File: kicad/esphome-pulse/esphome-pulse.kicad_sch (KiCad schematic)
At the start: 3 parts, among them J2 AudioJack2_Ground

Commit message: Sent to production
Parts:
- removed D1: APA-106-F5, LED_THT:LED_D5.0mm-4_RGB_Staggered_Pins, symbol LED:APA-106-F5
- added D3: WS2812B_THT, LED_THT:LED_D5.0mm-4_RGB_Staggered_Pins, symbol LED:NeoPixel_THT
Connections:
- net +5V: now also D3.4 (VDD)
- net GND: now also D3.2 (GND)
- net at U1.9 (A1CH8/TCH9/GPIO9): now also D3.1 (DIN)
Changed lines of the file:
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@@
 	)
 	(junction
-		(at 193.04 114.3)
+		(at 193.04 123.19)
 		(diameter 0)
 		(color 0 0 0 0)
@@
 	)
 	(no_connect
-		(at 212.09 104.14)
-	)
-	(no_connect
 		(at 93.98 82.55)
 	)
@@
 	)
 	(no_connect
+		(at 212.09 109.22)
+	)
+	(no_connect
 		(at 160.02 93.98)
 	)
@@
 	(wire
 		(pts
-			(xy 179.07 43.18) (xy 179.07 104.14)
-		)
-		(stroke
-			(width 0)
-			(type default)
-		)
-	)
-	(wire
-		(pts
-			(xy 193.04 114.3) (xy 204.47 114.3)
+			(xy 193.04 123.19) (xy 204.47 123.19)
+		)
+		(stroke
+			(width 0)
+			(type default)
+		)
+	)
+	(wire
+		(pts
+			(xy 179.07 43.18) (xy 179.07 109.22)
 		)
 		(stroke
@@
 	(wire
 		(pts
-			(xy 179.07 104.14) (xy 196.85 104.14)
-		)
-		(stroke
-			(width 0)
-			(type default)
-		)
-	)
-	(wire
-		(pts
-			(xy 193.04 77.47) (xy 193.04 114.3)
+			(xy 193.04 123.19) (xy 193.04 143.51)
 		)
 		(stroke
@@
 	(wire
 		(pts
-			(xy 204.47 96.52) (xy 204.47 99.06)
+			(xy 204.47 116.84) (xy 204.47 123.19)
 		)
 		(stroke
@@
 	(wire
 		(pts
+			(xy 204.47 96.52) (xy 204.47 101.6)
+		)
+		(stroke
+			(width 0)
+			(type default)
+		)
+	)
+	(wire
+		(pts
 			(xy 129.54 143.51) (xy 193.04 143.51)
 		)
@@
 	(wire
 		(pts
+			(xy 179.07 109.22) (xy 196.85 109.22)
+		)
+		(stroke
+			(width 0)
+			(type default)
+		)
+	)
+	(wire
+		(pts
 			(xy 129.54 139.7) (xy 129.54 143.51)
 		)
@@
 	(wire
 		(pts
-			(xy 193.04 143.51) (xy 193.04 114.3)
+			(xy 193.04 77.47) (xy 193.04 123.19)
 		)
 		(stroke
@@
 	)
 	(symbol
-		(lib_id "LED:APA-106-F5")
-		(at 204.47 106.68 0)
-		(unit 1)
-		(exclude_from_sim no)
-		(in_bom yes)
-		(on_board yes)
-		(dnp no)
-		(fields_autoplaced yes)
-		(property "Reference" "D1"
-			(at 217.17 97.7198 0)
-			(effects
-				(font
-					(size 1.27 1.27)
-				)
-			)
-		)
-		(property "Value" "APA-106-F5"
-			(at 217.17 100.2598 0)
-			(effects
-				(font
-					(size 1.27 1.27)
-				)
-			)
-		)
-		(property "Footprint" "LED_THT:LED_D5.0mm-4_RGB_Staggered_Pins"
-			(at 205.74 114.3 0)
-			(effects
-				(font
-					(size 1.27 1.27)
-				)
-				(justify left top)
-				(hide yes)
-			)
-		)
-		(property "Datasheet" "https://cdn.sparkfun.com/datasheets/Components/LED/COM-12877.pdf"
-			(at 207.01 116.205 0)
-			(effects
-				(font
-					(size 1.27 1.27)
-				)
-				(justify left top)
-				(hide yes)
-			)
-		)
-		(property "Description" "RGB LED with integrated controller, 5mm Package"
-			(at 204.47 106.68 0)
-			(effects
-				(font
-					(size 1.27 1.27)
-				)
-				(hide yes)
-			)
-		)
-		(pin "1"
-		)
-		(pin "2"
-		)
-		(pin "3"
-		)
-		(pin "4"
-		)
-		(instances
-			(project ""
-				(path "/236085cd-1dc4-4e54-9986-bb234567d56c"
-					(reference "D1")
-					(unit 1)
-				)
-			)
-		)
-	)
-	(symbol
 		(lib_id "Connector_Audio:AudioJack2_Ground")
 		(at 205.74 52.07 0)
@@
 					(unit 1)
 				)
+			)
+		)
+	)
+	(symbol
+		(lib_id "LED:NeoPixel_THT")
+		(at 204.47 109.22 0)
+		(unit 1)
+		(exclude_from_sim no)
+		(in_bom yes)
+		(on_board yes)
+		(dnp no)
+		(fields_autoplaced yes)
+		(property "Reference" "D3"
+			(at 217.17 102.7998 0)
+			(effects
+				(font
+					(size 1.27 1.27)
+				)
+			)
+		)
+		(property "Value" "WS2812B_THT"
+			(at 217.17 105.3398 0)
+			(effects
+				(font
+					(size 1.27 1.27)
+				)
+			)
+		)
+		(property "Footprint" "LED_THT:LED_D5.0mm-4_RGB_Staggered_Pins"
+			(at 205.74 116.84 0)
+			(effects
+				(font
+					(size 1.27 1.27)
+				)
+				(justify left top)
+				(hide yes)
+			)
+		)
+		(property "Datasheet" ""
+			(at 207.01 118.745 0)
+			(effects
+				(font
+					(size 1.27 1.27)
+				)
+				(justify left top)
+				(hide yes)
+			)
+		)
+		(property "Description" "RGB LED with integrated controller, 5mm/8mm LED package"
+			(at 204.47 109.22 0)
+			(effects
+				(font
+					(size 1.27 1.27)
+				)
+				(hide yes)
+			)
+		)
+		(pin "2"
+		)
+		(pin "3"
+		)
+		(pin "4"
+		)
+		(pin "1"
+		)
+		(instances
+			(project ""
+				(path "/236085cd-1dc4-4e54-9986-bb234567d56c"
+					(reference "D3")
+					(unit 1)
+				)

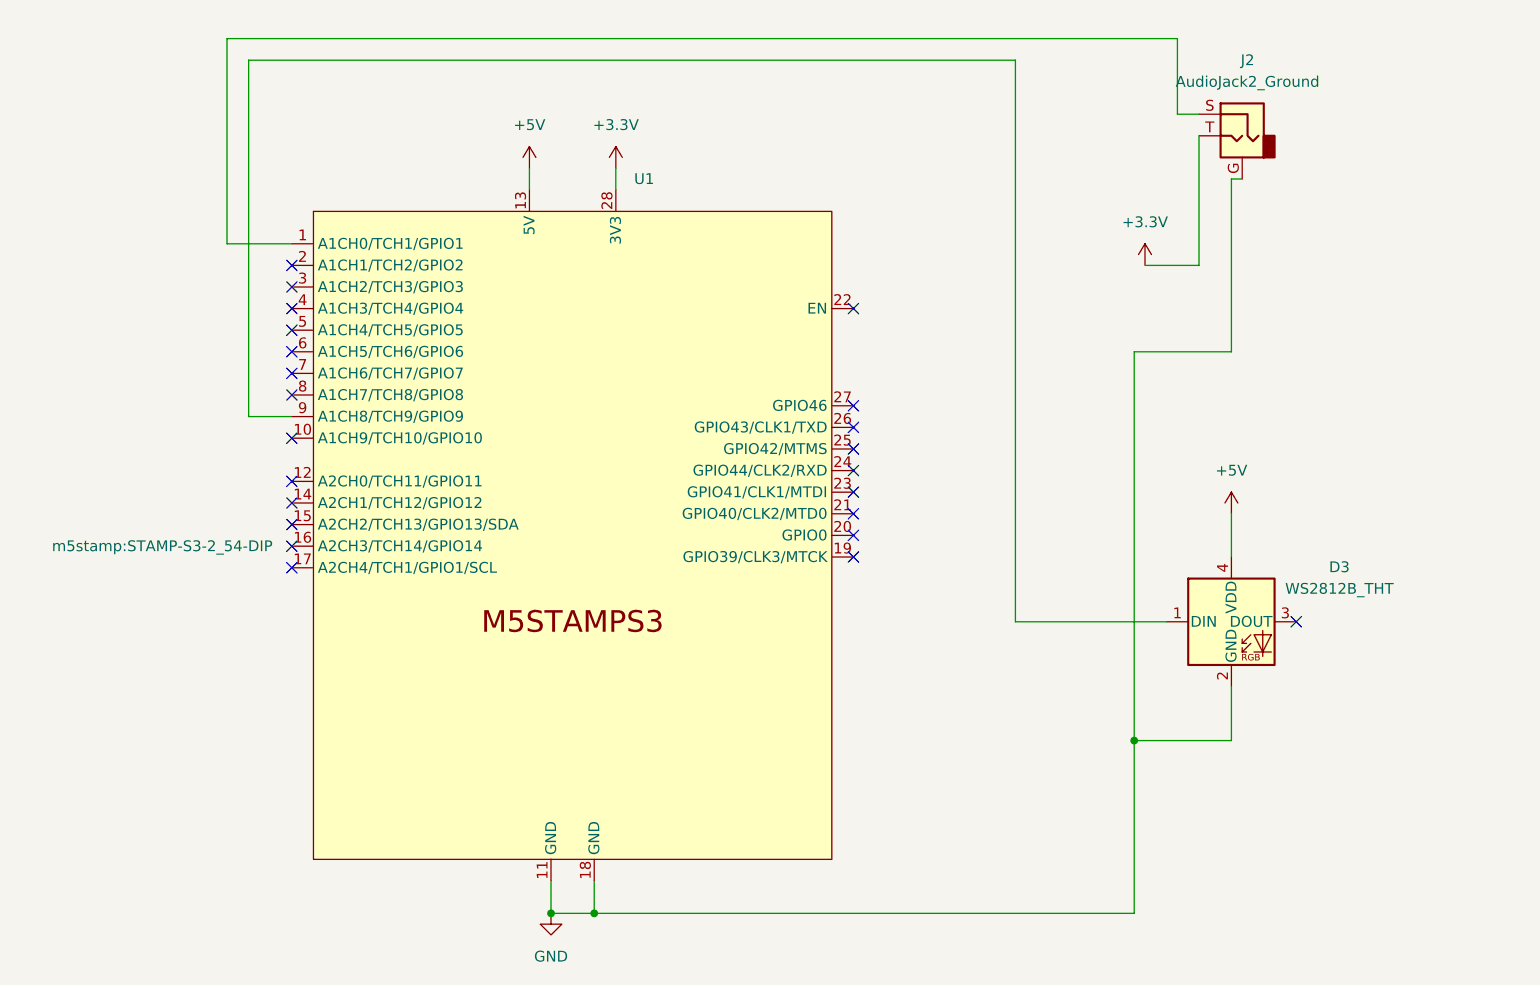
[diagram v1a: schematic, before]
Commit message: Add second version of PCB with smaller barrel jack
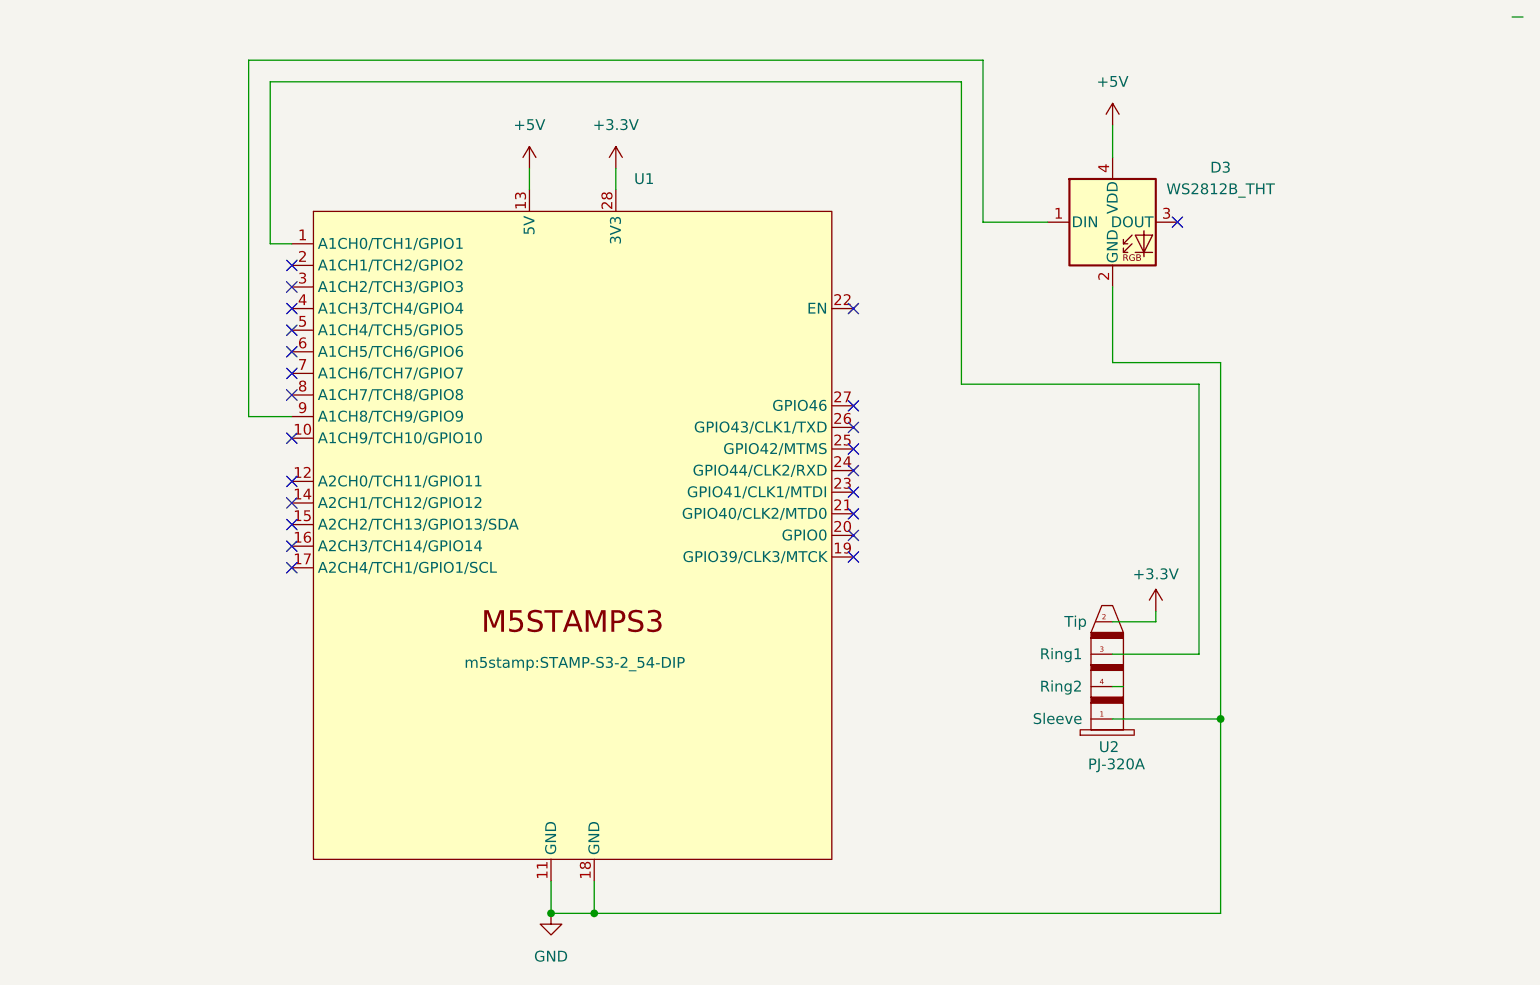
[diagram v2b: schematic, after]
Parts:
- removed J2: AudioJack2_Ground, Connector_Audio:Jack_3.5mm_CUI_SJ1-3523N_Horizontal, symbol Connector_Audio:AudioJack2_Ground
- added U2: PJ-320A, nathanhborger-PJ-320A:PJ-320A, symbol nathanhborger-PJ-320A:PJ-320A
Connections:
- net +3.3V: now also U2.2 (Tip)
- net GND: now also U2.1 (Sleeve)
- net at U1.1 (A1CH0/TCH1/GPIO1): now also U2.3 (Ring1)
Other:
- title: (none) -> ESPHome Pulse
- moved on the sheet: D3
